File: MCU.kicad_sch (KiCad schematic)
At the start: 16 parts

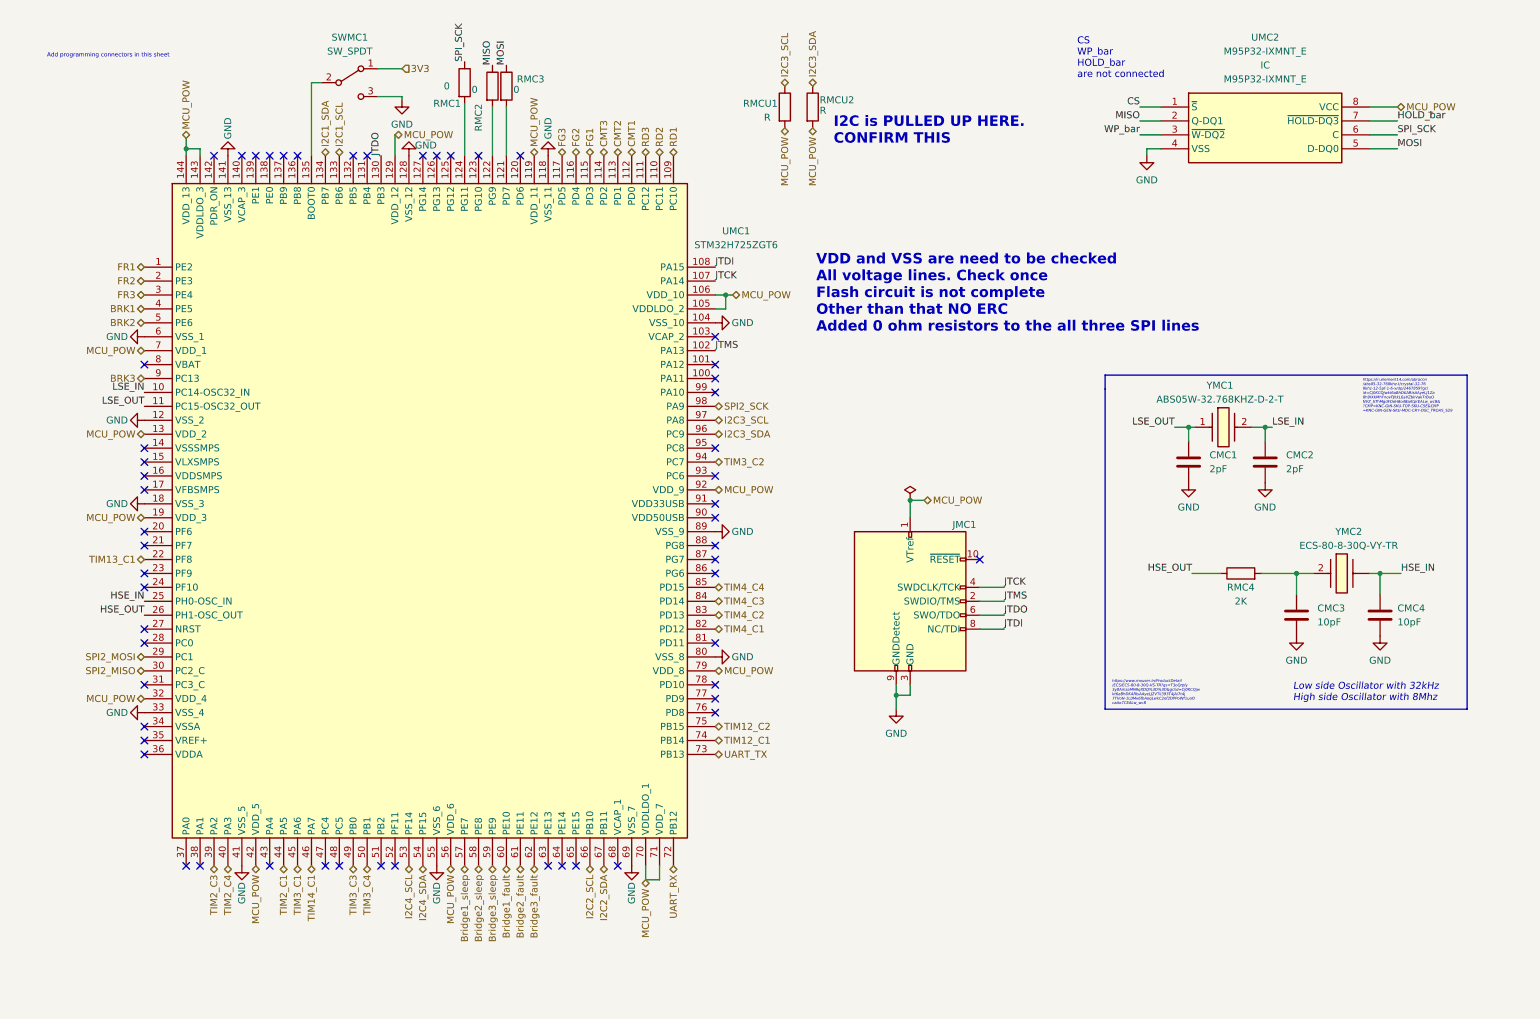
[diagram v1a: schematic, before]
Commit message: I2C lines are pulled up
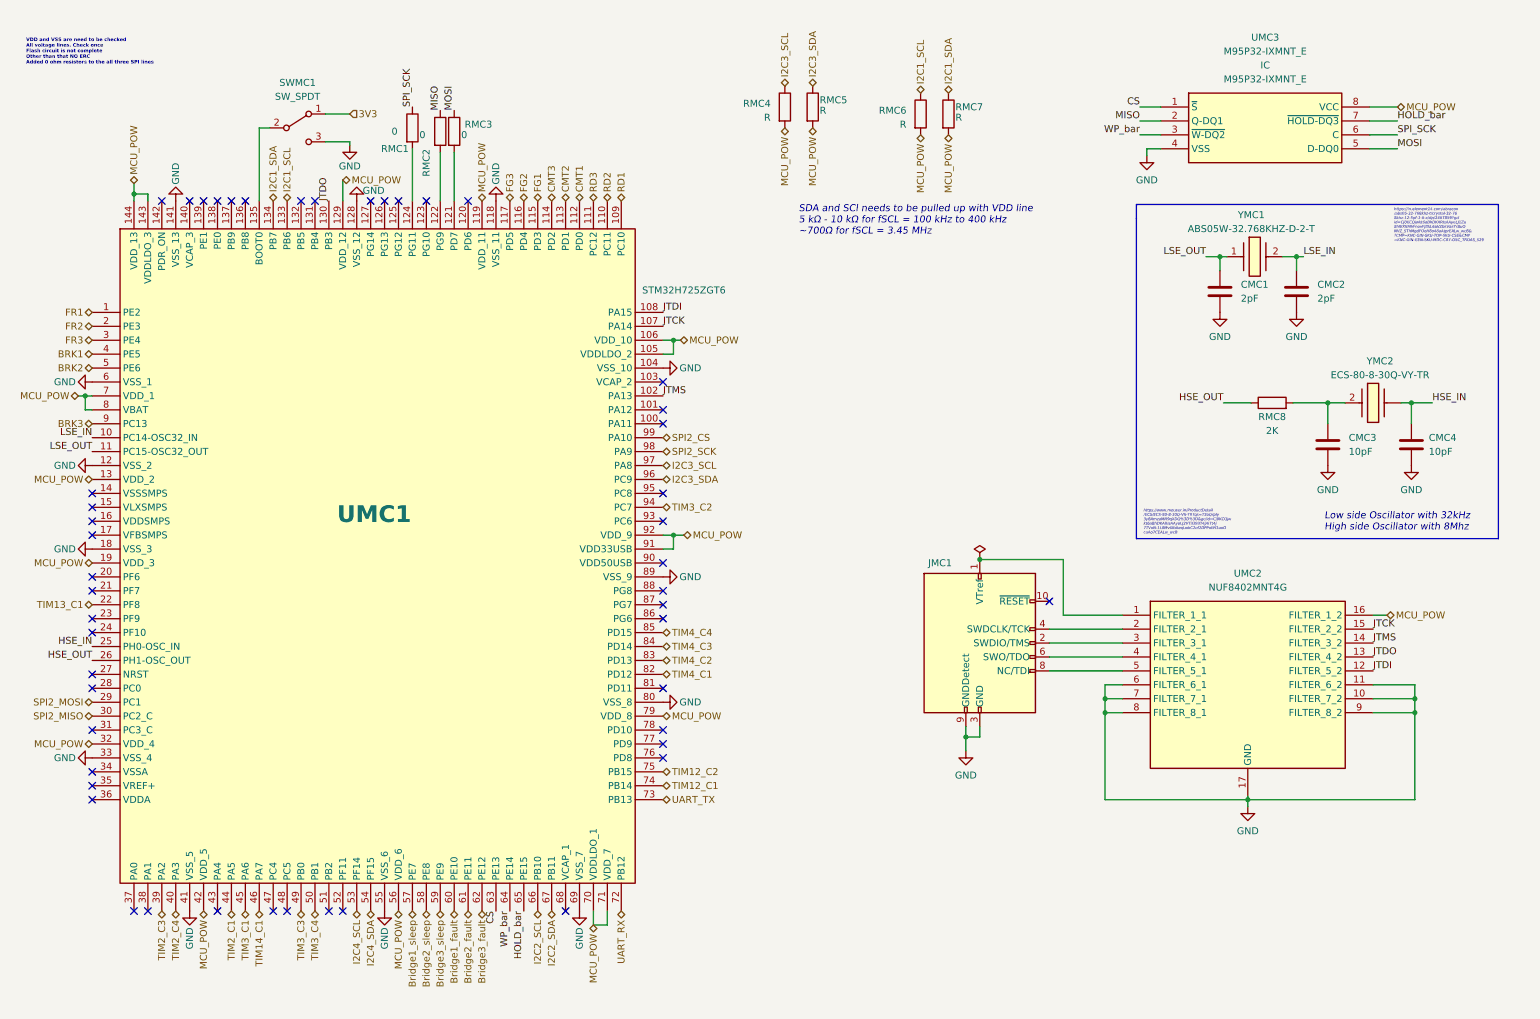
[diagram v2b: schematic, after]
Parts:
- added RMC6, RMC7: R, Resistor_SMD:R_0603_1608Metric, symbol Device:R
- added UMC2: NUF8402MNT4G, NUF8402MNT4G:SON50P160X400X100-17N, symbol NUF8402MNT4G:NUF8402MNT4G
- CMC1, CMC2, CMC3, CMC4: footprint Capacitor_SMD:C_0402_1005Metric -> Capacitor_SMD:C_0603_1608Metric
- RMC1, RMC2, RMC3: footprint (none) -> Resistor_SMD:R_0603_1608Metric
- RMC4: renamed from RMCU1; footprint (none) -> Resistor_SMD:R_0603_1608Metric
- RMC5: renamed from RMCU2; footprint (none) -> Resistor_SMD:R_0603_1608Metric
- renumbered RMC4 to RMC8, UMC2 to UMC3
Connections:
- net CS: now also UMC1.63 (PE13)
- net GND: now also UMC2.10 (FILTER_7_2), UMC2.11 (FILTER_6_2), UMC2.17 (GND), UMC2.6 (FILTER_6_1), UMC2.7 (FILTER_7_1), UMC2.8 (FILTER_8_1), UMC2.9 (FILTER_8_2)
- net HOLD_bar: now also UMC1.65 (PE15)
- net I2C1_SCL: now also RMC6.1
- net I2C1_SDA: now also RMC7.1
- net JTCK: now also UMC2.15 (FILTER_2_2); no longer JMC1.4 (SWDCLK/TCK)
- net JTDI: now also UMC2.12 (FILTER_5_2); no longer JMC1.8 (NC/TDI)
- net JTDO: now also UMC2.13 (FILTER_4_2); no longer JMC1.6 (SWO/TDO)
- net JTMS: now also UMC2.14 (FILTER_3_2); no longer JMC1.2 (SWDIO/TMS)
- net MCU_POW: now also UMC1.8 (VBAT), UMC1.91 (VDD33USB), RMC6.2, RMC7.2, UMC2.16 (FILTER_1_2); no longer JMC1.1 (VTref)
- net WP_bar: now also UMC1.64 (PE14)
- net SPI2_CS: now reaches UMC1.99 (PA10)
- new net: JMC1.1 (VTref), UMC2.1 (FILTER_1_1)
- new net: JMC1.2 (SWDIO/TMS), UMC2.3 (FILTER_3_1)
- new net: JMC1.4 (SWDCLK/TCK), UMC2.2 (FILTER_2_1)
- new net: JMC1.6 (SWO/TDO), UMC2.4 (FILTER_4_1)
- new net: JMC1.8 (NC/TDI), UMC2.5 (FILTER_5_1)
- no-connect marks 55 -> 49
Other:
- note added: "SDA and SCl needs to be pulled up with VDD line 5 kΩ - 10 kΩ for fSCL = 100 kHz to 400 kHz ~700Ω for fSCL = 3.45 MHz"
- note removed: "Add programming connectors in this sheet"
- note removed: "CS WP_bar HOLD_bar are not connected"
- note removed: "I2C is PULLED UP HERE. CONFIRM THIS"
- moved on the sheet: CMC1, CMC2, CMC3, CMC4, JMC1, RMC1, RMC2, RMC3, RMC8, SWMC1, UMC1, YMC1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

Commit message: Final Schematic
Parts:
- JMC1: footprint (none) -> SamacSys_Parts:FTSH10501LDVK
- SWMC1: footprint (none) -> Button_Switch_THT:SW_Push_1P2T_Vertical_E-Switch_800UDP8P1A1M6
- UMC3: footprint (none) -> M95P32-IXMNT_E:SOIC127P600X175-8N
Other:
- note removed: "VDD and VSS are need to be checked All voltage lines. Check once Flash circuit is not complete Other than that NO ERC Added 0 ohm resistors to the all three SPI lines"
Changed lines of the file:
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@@
     (effects (font (size 0.5 0.5) italic) (justify left bottom))
-  )
-  (text "VDD and VSS are need to be checked\nAll voltage lines. Check once\nFlash circuit is not complete\nOther than that NO ERC\nAdded 0 ohm resistors to the all three SPI lines\n"
-    (at 13.97 20.32 0)
-    (effects (font (size 0.635 0.635) (thickness 0.381) bold) (justify left bottom))
   )
   (text "https://www.mouser.in/ProductDetail\n/ECS/ECS-80-8-30Q-VS-TR?qs=T3oQrply\n3y8AmzaMN9qXDQ%3D%3D&gclid=Cj0KCQjw\nkt6aBhDKARIsAAyeLJ2VTiI393T4jAi7t4j\n7TVoN-1L0Mv6fbAeqLwkC2of2DPPoWf1uoO\ncaAo7CEALw_wcB"
@@
       (effects (font (size 1.27 1.27)) (justify right) hide)
     )
-    (property "Footprint" "" (id 2) (at 187.96 125.73 0)
+    (property "Footprint" "SamacSys_Parts:FTSH10501LDVK" (id 2) (at 187.96 125.73 0)
       (effects (font (size 1.27 1.27)) hide)
     )
@@
     (property "Reference" "SWMC1" (id 0) (at 63.5 23.495 0))
     (property "Value" "SW_SPDT" (id 1) (at 63.5 26.035 0))
-    (property "Footprint" "" (id 2) (at 63.5 31.75 0)
+    (property "Footprint" "Button_Switch_THT:SW_Push_1P2T_Vertical_E-Switch_800UDP8P1A1M6" (id 2) (at 63.5 31.75 0)
       (effects (font (size 1.27 1.27)) hide)
     )
@@
     (property "Reference" "UMC3" (id 0) (at 240.03 15.24 0))
     (property "Value" "M95P32-IXMNT_E" (id 1) (at 240.03 17.78 0))
-    (property "Footprint" "" (id 2) (at 220.98 27.94 0)
-      (effects (font (size 1.27 1.27)) hide)
-    )
+    (property "Footprint" "M95P32-IXMNT_E:SOIC127P600X175-8N" (id 2) (at 220.98 27.94 0)
+      (effects (font (size 1.27 1.27)) hide)
+    )

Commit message: MCU circuitry forgot LOL
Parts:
- added CMC1: 1u, Capacitor_SMD:C_0603_1608Metric, symbol Device:C
- added CMC10: 20u, Capacitor_SMD:C_0603_1608Metric, symbol Device:C
- added CMC11, CMC12: 2.2u, Capacitor_SMD:C_0603_1608Metric, symbol Device:C
- added CMC2, CMC5: 100n, Capacitor_SMD:C_0603_1608Metric, symbol Device:C
- added CMC8: 4.7u, Capacitor_SMD:C_0603_1608Metric, symbol Device:C
- added CMC9: 220p, Capacitor_SMD:C_0603_1608Metric, symbol Device:C
- added CMCB1, CMCB2, CMCB3, CMCB4, CMCB5, CMCB6, CMCB7, CMCB8: 4.7u, Capacitor_SMD:C_0805_2012Metric, symbol Device:C
- added CMCD1, CMCD7: 4.7u, Capacitor_SMD:C_0402_1005Metric, symbol Device:C
- added CMCD10, CMCD11, CMCD12, CMCD2, CMCD3, CMCD4, CMCD5, CMCD6, CMCD8, CMCD9: 100n, Capacitor_SMD:C_0402_1005Metric, symbol Device:C
- added LMC1: 2.2u, Inductor_SMD:L_0805_2012Metric_Pad1.15x1.40mm_HandSolder, symbol Device:L
- added RMC8: 10k, Resistor_SMD:R_0603_1608Metric, symbol Device:R
- renumbered CMC1 to CMC3, CMC2 to CMC4, CMC3 to CMC6, CMC4 to CMC7, RMC4 to RMC1, RMC5 to RMC2, RMC1 to RMC3, RMC2 to RMC4, RMC3 to RMC5, RMC8 to RMC9, UMC3 to UMC2, UMC2 to UMC3
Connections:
- net 3V3 is gone; now on net MCU_POW: SWMC1.1 (A)
- net GND: now also UMC1.14 (VSSSMPS), UMC1.34 (VSSA), CMC1.2, CMC10.2, CMC11.2, CMC12.2, CMC2.2, CMC5.2, CMC8.2, CMC9.2, CMCB1.2, CMCB2.2, CMCB3.2, CMCB4.2, CMCB5.2, CMCB6.2, CMCB7.2, CMCB8.2, CMCD1.2, CMCD10.2, CMCD11.2, CMCD12.2, CMCD2.2, CMCD3.2, CMCD4.2, CMCD5.2, CMCD6.2, CMCD7.2, CMCD8.2, CMCD9.2
- net MCU_POW: now also UMC1.142 (PDR_ON), UMC1.16 (VDDSMPS), CMC1.1, CMC2.1, CMC8.1, CMCB1.1, CMCB2.1, CMCB3.1, CMCB4.1, CMCB5.1, CMCB6.1, CMCB7.1, CMCB8.1, CMCD1.1, CMCD10.1, CMCD11.1, CMCD12.1, CMCD2.1, CMCD3.1, CMCD4.1, CMCD5.1, CMCD6.1, CMCD7.1, CMCD8.1, CMCD9.1; no longer UMC1.105 (VDDLDO_2), UMC1.143 (VDDLDO_3), UMC1.70 (VDDLDO_1)
- net VCAP2: now reaches UMC1.103 (VCAP_2)
- net VCAP2: now also UMC1.140 (VCAP_3), CMC12.1
- net at SWMC1.2 (B): now also RMC8.2; no longer UMC1.135 (BOOT0)
- net VLXSMPS: now reaches UMC1.15 (VLXSMPS)
- net VLXSMPS: now also CMC9.1, LMC1.2
- net VDDLDO: now reaches UMC1.17 (VFBSMPS)
- net VDDLDO: now also UMC1.105 (VDDLDO_2), UMC1.143 (VDDLDO_3), UMC1.70 (VDDLDO_1), CMC10.1, LMC1.1
- net reset: now reaches UMC1.27 (NRST)
- net reset: now also JMC1.10 (~{RESET}), CMC5.1
- net VCAP1: now reaches UMC1.68 (VCAP_1)
- net VCAP1: now also CMC11.1
- new net switch_1: RMC8.1, UMC1.135 (BOOT0)
- no-connect marks 49 -> 38
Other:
- note added: "The 4.7uF capacitor is the Bulk decoupling capacitor. Place it close to the VDD VSS pins. The rest of the decoupling is through the other caps and pwr and gnd planes."
- title: AOCS BOARD -> MCU Schematic
- moved on the sheet: CMC3, CMC4, CMC6, CMC7, JMC1, RMC1, RMC2, RMC3, RMC4, RMC5, RMC6, RMC7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

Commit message: MCU updated
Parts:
- removed CMC10: 20u, Capacitor_SMD:C_0603_1608Metric, symbol Device:C
- added CMC13, CMC14, CMC15: 10u, symbol Device:C
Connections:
- net GND: now also CMC13.2, CMC14.2, CMC15.2
- net MCU_POW: now also CMC15.1
- net VDDLDO: now also CMC13.1, CMC14.1
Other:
- note added: "Connect Mounting leds to ground"
- note added: "ESR 10m"
- note added: "ESR 5m"
- note added: "PCM12SMTBR"

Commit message: inductor part numbers added
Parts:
- removed LMC1: 2.2u, Inductor_SMD:L_0805_2012Metric_Pad1.15x1.40mm_HandSolder, symbol Device:L
- added CMC0: 100n, Capacitor_SMD:C_0603_1608Metric, symbol Device:C
- added LMC1: 74438336022, symbol 74438336022:74438336022
- CMC1: value 1u -> 4.7u
- CMC13, CMC14, CMC15: footprint (none) -> Capacitor_SMD:C_0603_1608Metric
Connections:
- net GND: now also UMC1.142 (PDR_ON), CMC0.2
- net MCU_POW: now also CMC0.1; no longer SWMC1.1 (A), UMC1.142 (PDR_ON)
- net VDDLDO: now also LMC1.1
- net VLXSMPS: now also LMC1.2
- new net ADCS_BOOT_MODE: SWMC1.1 (A)
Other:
- note added: "All of these decaps should be low ESR Ceramic caps"
- note added: "C0603C106M9PACTU"
- note added: "Place atleast one 100nF on each VDDxxx pin"
- note added: "Please add TP to the SPI lines connected to interboard"
- note removed: "ESR 10m"
- note removed: "ESR 5m"
- moved on the sheet: CMC9

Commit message: PDR corrected
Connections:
- net GND: no longer UMC1.142 (PDR_ON)
- net MCU_POW: now also UMC1.142 (PDR_ON)

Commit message: All frequency sensitive caps and specific inductor PNs added
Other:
- note added: "GRM188R71A225KE15D"
- note added: "MC0603N221K500CT"
- note added: "Please add PN for crystal caps"
- note added: "Please choose appropriate PN for these decaps"
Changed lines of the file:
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@@
     (stroke (width 0) (type default) (color 0 0 0 0))
+  )
+  (text "Please choose appropriate PN for these decaps " (at 292.1 212.09 0)
+    (effects (font (size 1.27 1.27)) (justify left bottom))
   )
   (text "Connect Mounting leds to ground\n" (at 48.26 101.6 0)
@@
   )
   (text "\n    C0603C106M9PACTU" (at 58.42 215.9 0)
+    (effects (font (size 1.27 1.27)) (justify left bottom))
+  )
+  (text "Please add PN for crystal caps\n" (at 302.26 170.18 0)
     (effects (font (size 1.27 1.27)) (justify left bottom))
   )
@@
     (effects (font (size 1.27 1.27)) (justify left bottom))
   )
+  (text "MC0603N221K500CT " (at 63.5 173.99 0)
+    (effects (font (size 1.27 1.27)) (justify left bottom))
+  )
   (text "SDA and SCl needs to be pulled up with VDD line\n5 kΩ - 10 kΩ for fSCL = 100 kHz to 400 kHz\n~700Ω for fSCL = 3.45 MHz\n"
     (at 351.79 44.45 0)
     (effects (font (size 1.27 1.27) italic) (justify left bottom))
+  )
+  (text "GRM188R71A225KE15D" (at 25.4 208.28 0)
+    (effects (font (size 1.27 1.27)) (justify left bottom))
   )
   (text "Please add TP to the SPI lines connected to interboard\n"
@@
     (effects (font (size 0.762 0.762) italic) (justify left bottom))
   )
+  (text "GRM188R71A225KE15D" (at 43.18 208.28 0)
+    (effects (font (size 1.27 1.27)) (justify left bottom))
+  )
   (text "https://www.mouser.in/ProductDetail\n/ECS/ECS-80-8-30Q-VS-TR?qs=T3oQrply\n3y8AmzaMN9qXDQ%3D%3D&gclid=Cj0KCQjw\nkt6aBhDKARIsAAyeLJ2VTiI393T4jAi7t4j\n7TVoN-1L0Mv6fbAeqLwkC2of2DPPoWf1uoO\ncaAo7CEALw_wcB"
